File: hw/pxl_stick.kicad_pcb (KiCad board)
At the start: 2 copper layers, 25 x 99.9 mm, 69 parts, among them J1 Conn_01x02, J2 Conn_01x06_Socket, J3 Conn_01x01_Socket, J4 Conn_01x01, Q1 IRLML6244, Q2 IRLML6244, U1 AP2112K-3.3, U2 TSOP75438WTT, U3 INMP441ACEZ-R7, U4 ESP32-WROOM-E, U5 SN74LVC1T45DCK

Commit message: Version 1.1 changes
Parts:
- removed the G*** at (73.5, 55.5)
- removed the G*** at (69.6, 119.5)
- removed the G*** at (73.4, 119.4)
- removed the G*** at (81.0, 119.4)
- removed the G*** at (84.4, 99.7)
- removed NT3: NetTie_2, NetTie_Vasil:NetTie-2_SMD_Pad0.20mm
- removed the R5 at (66.5, 71.0)
- removed R6, R7: 510, Resistor_SMD:R_0805_2012Metric_Pad1.20x1.40mm_HandSolder
- removed TP1, TP2, TP3, TP8: TestPoint, TestPoint:TestPoint_Pad_1.0x1.0mm
- added C14: 100n, Capacitor_SMD:C_0805_2012Metric_Pad1.18x1.45mm_HandSolder, F.Cu at (62.4, 95.3)
- added R11: 20k, Resistor_SMD:R_0805_2012Metric_Pad1.20x1.40mm_HandSolder, F.Cu at (62.4, 99.1)
- added R12: 20k, Resistor_SMD:R_0805_2012Metric_Pad1.20x1.40mm_HandSolder, F.Cu at (84.5, 95.3)
- added ss1: qr, LOGO, B.Cu at (73.4, 50.5)
- C15: renamed from C14; value 100n -> 470n
- C16: renamed from C15; value 100n -> 470n
- J1: footprint Connector_Wire:SolderWire-0.15sqmm_1x02_P4mm_D0.5mm_OD1.5mm -> Connector_Wire:SolderWire-0.5sqmm_1x02_P4.6mm_D0.9mm_OD2.1mm
- J4: footprint Connector_Wire:SolderWire-0.15sqmm_1x01_D0.5mm_OD1.5mm -> Connector_Wire:SolderWire-0.5sqmm_1x01_D0.9mm_OD2.1mm
- R1: value 330 -> 470
- R15: renamed from R13; value 33 -> 430
- ss2: renamed from G***; value LOGO -> wled logo
- ss3: renamed from G***; value LOGO -> ws281x signal
- ss4: renamed from G***; value LOGO -> brightness
- ss5: renamed from G***; value LOGO -> palette
- ss6: renamed from G***; value LOGO -> reset
- ss7: renamed from G***; value LOGO -> bootloader
- moved C10 16.9 mm to (80.0, 71.1), turned to 90 degrees
- moved ss4 5.35 mm to (71.1, 119.8)
- moved G*** 4.46 mm to (78.3, 108.8)
- moved C9 3.65 mm to (66.7, 71.1), turned to 90 degrees
- moved ss5 1.50 mm to (75.7, 119.8)
- moved SW3 0.29 mm to (73.4, 58.0)
- moved ss3 0.24 mm to (78.4, 104.1)
- moved ss7 0.06 mm to (84.5, 91.8)
- turned JP2 to 90 degrees
- renumbered R11 to R13, R12 to R14, R2 to R3, R3 to R4, R4 to R5
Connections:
- D1 pad 2: +3V3 -> /MCU/LED
- SW1 pad 1: Net-(R5-Pad2) -> TB1
- SW2 pad 1: Net-(R6-Pad2) -> TB2
- SW3 pad 1: Net-(R7-Pad2) -> TB3
- U4 pad 13: unconnected-(U4-MTMS/GPIO14/ADC2_CH6-Pad13) -> TB3
- U4 pad 24: unconnected-(U4-ADC2_CH2/GPIO2-Pad24) -> /MCU/LED
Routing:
- net TB3: track 18.3 -> 61.1 mm, vias 0 -> 4
- net Net-(R6-Pad2): track 35.1 -> 0.00 mm
- net Net-(R5-Pad2): track 35.0 -> 0.00 mm
- net GND: track 115.3 -> 87.7 mm, vias 28 -> 21
- net Net-(R7-Pad2): track 24.2 -> 0.00 mm
- net TB2: track 44.7 -> 68.4 mm
- net TB1: track 31.0 -> 50.4 mm
- net /MCU/LED: track 0.00 -> 15.5 mm
- net /MCU/MCU_BOOT: track 45.6 -> 38.7 mm
- net +3V3: track 69.7 -> 65.4 mm, vias 10 -> 13
- net Net-(U2-VS): track 15.2 -> 12.6 mm
- net /MCU/MCU_EN: track 24.0 -> 26.3 mm
- net /MCU/WS2812_3V3: track 9.83 -> 8.17 mm, vias 2 -> 0
- net RE2: track 58.2 -> 56.6 mm
- net REB: track 47.7 -> 46.3 mm
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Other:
- outline, holes or cut-outs redrawn
- board text added: "PXL"
- board text added: "PXLstick"
- board text added: "WS281x | GPIO 4 󰝣 | GPIO 32 󰔷 | GPIO 33 󰄰 | GPIO 14 RE 1 | GPIO 27 RE 2 | GPIO 16 RE BTN | GPIO 17 LED | GPIO 2 IR rec | GPIO 23 MIC SD | GPIO 15 MIC WS | GPIO 13 MIC SCK | GPIO 25"
- board text added: "github.com/VasilKalchev/PXLstick"
- board text added: "v${REVISION}"
- board text added: "v${REVISION} ${ISSUE_DATE}"
- board text removed: "WLED"
- board text removed: "WLED stick"
- board text removed: "r${REVISION}"
- board text removed: "r1.0 2023-06-11"

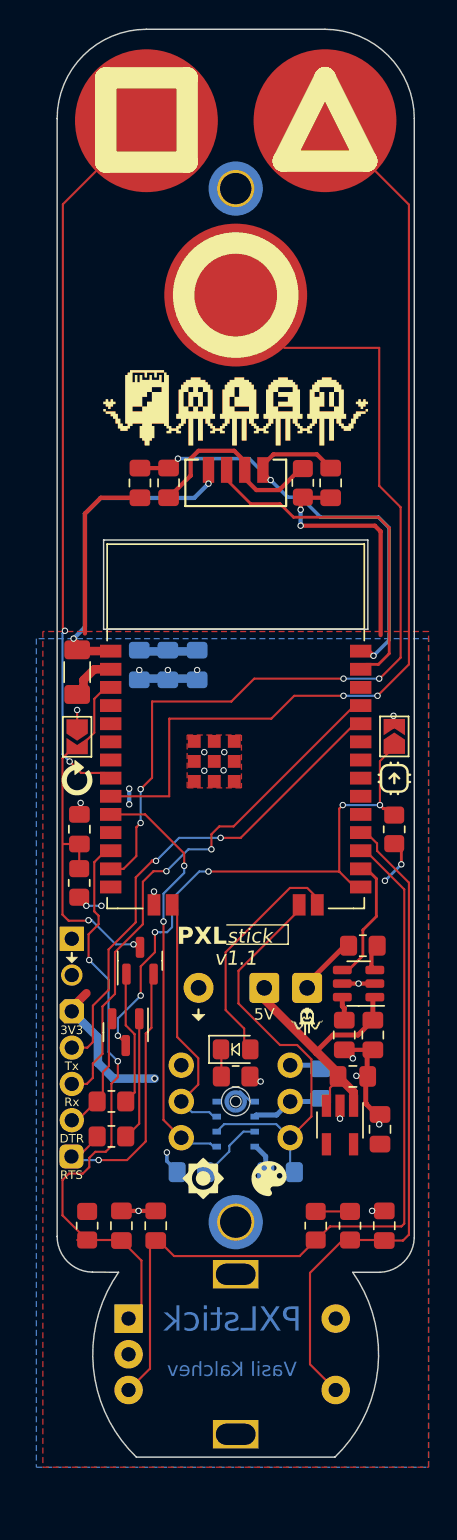
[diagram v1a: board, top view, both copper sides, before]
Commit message: Fix via annular width, remove netties
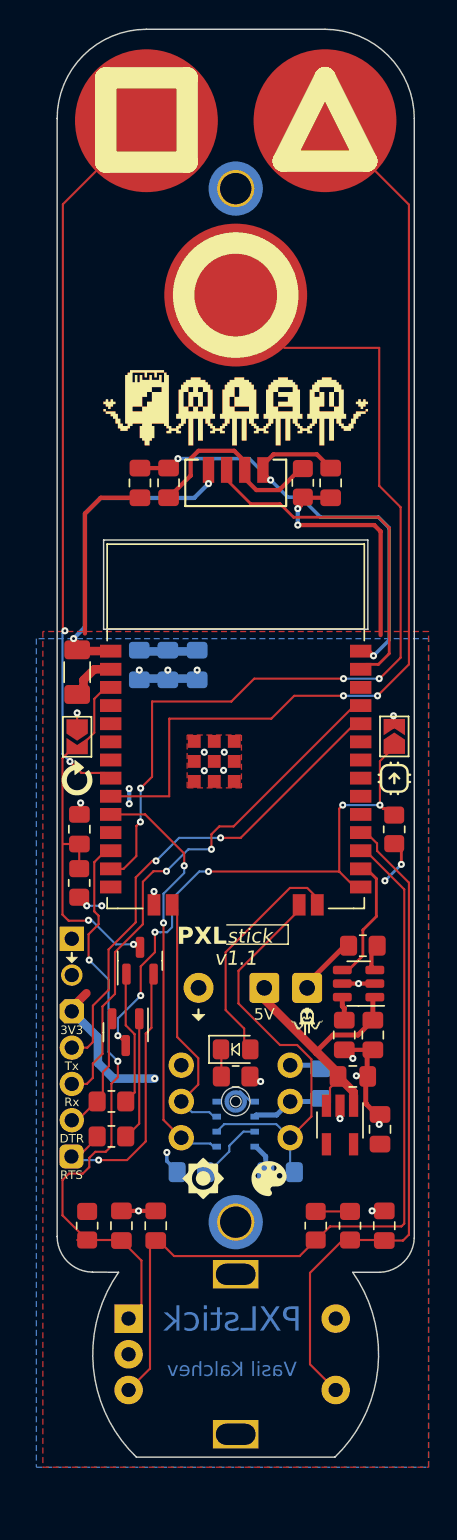
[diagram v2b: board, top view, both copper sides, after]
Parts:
- removed NT1, NT2: NetTie_2, NetTie_Vasil:NetTie-2_SMD_Pad0.20mm
- R13, R14, R3, R4, R5, R9: value 10k -> 20k
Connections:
- J2 pad 4: /MCU/SERIAL_TX -> /MCU/MCU_RX
- J2 pad 5: /MCU/SERIAL_RX -> /MCU/MCU_TX
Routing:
- net /MCU/MCU_RX: track 31.5 -> 34.1 mm
- net /MCU/MCU_TX: track 34.8 -> 37.1 mm
- net /MCU/SERIAL_TX: track 2.13 -> 0.00 mm
- net /MCU/SERIAL_RX: track 1.93 -> 0.00 mm

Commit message: change smalles hole to 0.3mm
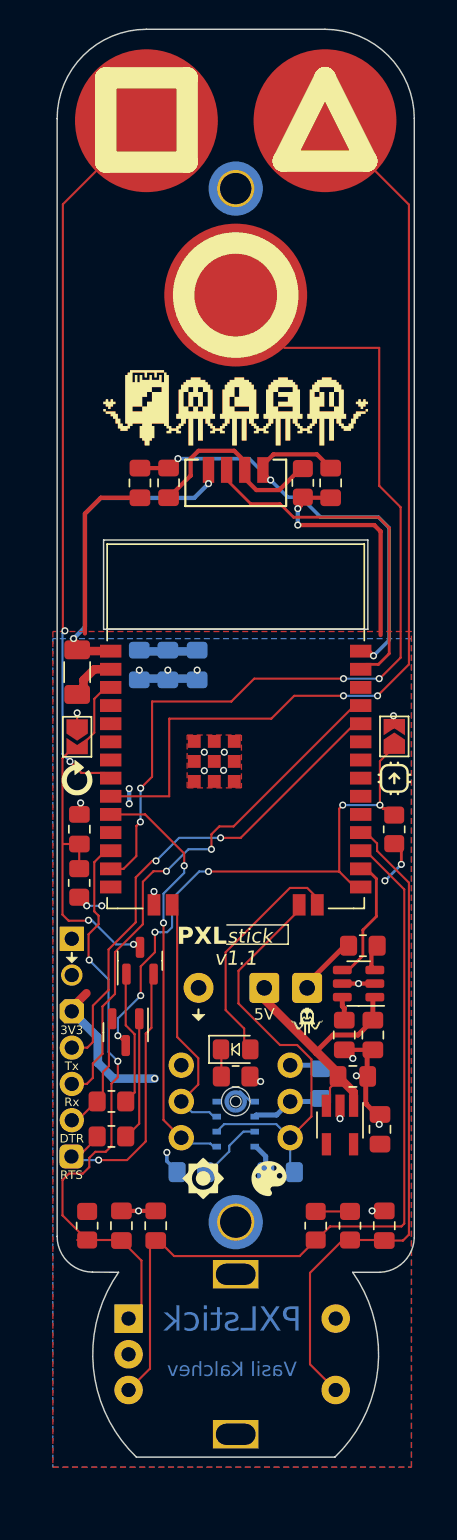
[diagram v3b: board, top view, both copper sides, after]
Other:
- board text removed: "Brightness | Speed | Intensity | Palette | Effect"
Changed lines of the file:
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@@
 				(material "Direct Printing")
 			)
-			(layer "F.Paste"
-				(type "Top Solder Paste")
-			)
 			(layer "F.Mask"
 				(type "Top Solder Mask")
@@
 				(loss_tangent 0)
 			)
-			(layer "B.Paste"
-				(type "Bottom Solder Paste")
-			)
 			(layer "B.SilkS"
 				(type "Bottom Silk Screen")
@@
 		)
 	)
-	(gr_text "Brightness | Speed | Intensity | Palette | Effect"
-		(at 167.9 130.9 0)
-		(layer "Cmts.User")
-		(effects
-			(font
-				(size 1 1)
-				(thickness 0.125)
-			)
-			(justify left bottom)
-		)
-	)
 	(dimension
 		(type aligned)
@@
 		(at 69.75 97.9)
 		(size 0.5)
-		(drill 0.2)
+		(drill 0.3)
 		(layers "F.Cu" "B.Cu")
 		(net 1)
@@
 		(at 68.3 101.9)
 		(size 0.5)
-		(drill 0.2)
+		(drill 0.3)
 		(layers "F.Cu" "B.Cu")
 		(net 1)
@@
 		(at 63.1 104.5)
 		(size 0.5)
-		(drill 0.2)
+		(drill 0.3)
 		(layers "F.Cu" "B.Cu")
 		(net 6)
@@
 		(at 65.104849 111.580973)
 		(size 0.5)
-		(drill 0.2)
+		(drill 0.3)
 		(layers "F.Cu" "B.Cu")
 		(net 6)
@@
 		(at 71.155349 89.944651)
 		(size 0.5)
-		(drill 0.2)
+		(drill 0.3)
 		(layers "F.Cu" "B.Cu")
 		(net 8)
@@
 		(at 62.5 93.5)
 		(size 0.5)
-		(drill 0.2)
+		(drill 0.3)
 		(layers "F.Cu" "B.Cu")
 		(net 8)
@@
 		(at 83.4 116)
 		(size 0.5)
-		(drill 0.2)
+		(drill 0.3)
 		(layers "F.Cu" "B.Cu")
 		(net 8)
@@
 		(at 62.005099 81.994901)
 		(size 0.5)
-		(drill 0.2)
+		(drill 0.3)
 		(layers "F.Cu" "B.Cu")
 		(net 8)
@@
 		(at 67.635349 99.7)
 		(size 0.5)
-		(drill 0.2)
+		(drill 0.3)
 		(layers "F.Cu" "B.Cu")
 		(net 8)
@@
 		(at 75.1 113)
 		(size 0.5)
-		(drill 0.2)
+		(drill 0.3)
 		(layers "F.Cu" "B.Cu")
 		(net 8)
@@
 		(at 80.655349 115.6)
 		(size 0.5)
-		(drill 0.2)
+		(drill 0.3)
 		(layers "F.Cu" "B.Cu")
 		(net 8)
@@
 		(at 69.3125 69.4)
 		(size 0.5)
-		(drill 0.2)
+		(drill 0.3)
 		(layers "F.Cu" "B.Cu")
 		(net 8)
@@
 		(at 81.8 112.6)
 		(size 0.5)
-		(drill 0.2)
+		(drill 0.3)
 		(layers "F.Cu" "B.Cu")
 		(net 8)
@@
 		(at 81.955349 106.144651)
 		(size 0.5)
-		(drill 0.2)
+		(drill 0.3)
 		(layers "F.Cu" "B.Cu")
 		(net 8)
@@
 		(at 83 83.2)
 		(size 0.5)
-		(drill 0.2)
+		(drill 0.3)
 		(layers "F.Cu" "B.Cu")
 		(net 8)
@@
 		(at 72.555349 89.944651)
 		(size 0.5)
-		(drill 0.2)
+		(drill 0.3)
 		(layers "F.Cu" "B.Cu")
 		(net 8)
@@
 		(at 72.505349 91.219651)
 		(size 0.5)
-		(drill 0.2)
+		(drill 0.3)
 		(layers "F.Cu" "B.Cu")
 		(net 8)
@@
 		(at 82.9 122.057151)
 		(size 0.5)
-		(drill 0.2)
+		(drill 0.3)
 		(layers "F.Cu" "B.Cu")
 		(net 8)
@@
 		(at 71.450349 71.149651)
 		(size 0.5)
-		(drill 0.2)
+		(drill 0.3)
 		(layers "F.Cu" "B.Cu")
 		(net 8)
@@
 		(at 62.255349 87.2)
 		(size 0.5)
-		(drill 0.2)
+		(drill 0.3)
 		(layers "F.Cu" "B.Cu")
 		(net 8)
@@
 		(at 75.8 70.9)
 		(size 0.5)
-		(drill 0.2)
+		(drill 0.3)
 		(layers "F.Cu" "B.Cu")
 		(net 8)
@@
 		(at 81.555349 111.382151)
 		(size 0.5)
-		(drill 0.2)
+		(drill 0.3)
 		(layers "F.Cu" "B.Cu")
 		(net 8)
@@
 		(at 71.155349 91.244651)
 		(size 0.5)
-		(drill 0.2)
+		(drill 0.3)
 		(layers "F.Cu" "B.Cu")
 		(net 8)
@@
 		(at 84.4 87.4)
 		(size 0.5)
-		(drill 0.2)
+		(drill 0.3)
 		(layers "F.Cu" "B.Cu")
 		(net 8)
@@
 		(at 66.555349 122.057151)
 		(size 0.5)
-		(drill 0.2)
+		(drill 0.3)
 		(layers "F.Cu" "B.Cu")
 		(net 8)
@@
 		(at 83.8 98.95)
 		(size 0.5)
-		(drill 0.2)
+		(drill 0.3)
 		(layers "F.Cu" "B.Cu")
 		(net 9)
@@
 		(at 70.655349 84.2)
 		(size 0.5)
-		(drill 0.2)
+		(drill 0.3)
 		(layers "F.Cu" "B.Cu")
 		(net 9)
@@
 		(at 77.7 74.05)
 		(size 0.5)
-		(drill 0.2)
+		(drill 0.3)
 		(layers "F.Cu" "B.Cu")
 		(net 9)
@@
 		(at 66.605349 84.2)
 		(size 0.5)
-		(drill 0.2)
+		(drill 0.3)
 		(layers "F.Cu" "B.Cu")
 		(net 9)
@@
 		(at 68.536638 117.963674)
 		(size 0.5)
-		(drill 0.2)
+		(drill 0.3)
 		(layers "F.Cu" "B.Cu")
 		(net 9)
@@
 		(at 68.605349 84.2)
 		(size 0.5)
-		(drill 0.2)
+		(drill 0.3)
 		(layers "F.Cu" "B.Cu")
 		(net 9)
@@
 		(at 63.980349 100.7)
 		(size 0.5)
-		(drill 0.2)
+		(drill 0.3)
 		(layers "F.Cu" "B.Cu")
 		(net 9)
@@
 		(at 84.95 97.8)
 		(size 0.5)
-		(drill 0.2)
+		(drill 0.3)
 		(layers "F.Cu" "B.Cu")
 		(net 9)
@@
 		(at 65.9 93.559651)
 		(size 0.5)
-		(drill 0.2)
+		(drill 0.3)
 		(layers "F.Cu" "B.Cu")
 		(net 9)
@@
 		(at 67.679849 112.794651)
 		(size 0.5)
-		(drill 0.2)
+		(drill 0.3)
 		(layers "F.Cu" "B.Cu")
 		(net 9)
@@
 		(at 65.9 92.5)
 		(size 0.5)
-		(drill 0.2)
+		(drill 0.3)
 		(layers "F.Cu" "B.Cu")
 		(free yes)
@@
 		(at 62.930349 100.7)
 		(size 0.5)
-		(drill 0.2)
+		(drill 0.3)
 		(layers "F.Cu" "B.Cu")
 		(net 9)
@@
 		(at 77.7 72.9)
 		(size 0.5)
-		(drill 0.2)
+		(drill 0.3)
 		(layers "F.Cu" "B.Cu")
 		(net 9)
@@
 		(at 63.761582 118.500884)
 		(size 0.5)
-		(drill 0.2)
+		(drill 0.3)
 		(layers "F.Cu" "B.Cu")
 		(net 19)
@@
 		(at 71.655349 96.744651)
 		(size 0.5)
-		(drill 0.2)
+		(drill 0.3)
 		(layers "F.Cu" "B.Cu")
 		(net 20)
@@
 		(at 68.505349 98.281438)
 		(size 0.5)
-		(drill 0.2)
+		(drill 0.3)
 		(layers "F.Cu" "B.Cu")
 		(net 20)
@@
 		(at 72.3 95.944651)
 		(size 0.5)
-		(drill 0.2)
+		(drill 0.3)
 		(layers "F.Cu" "B.Cu")
 		(net 21)
@@
 		(at 67.778112 97.556938)
 		(size 0.5)
-		(drill 0.2)
+		(drill 0.3)
 		(layers "F.Cu" "B.Cu")
 		(net 21)
@@
 		(at 83.284331 86.000578)
 		(size 0.5)
-		(drill 0.2)
+		(drill 0.3)
 		(layers "F.Cu" "B.Cu")
 		(net 28)
@@
 		(at 80.9 86)
 		(size 0.5)
-		(drill 0.2)
+		(drill 0.3)
 		(layers "F.Cu" "B.Cu")
 		(net 28)
@@
 		(at 66.7 92.467326)
 		(size 0.5)
-		(drill 0.2)
+		(drill 0.3)
 		(layers "F.Cu" "B.Cu")
 		(net 29)
@@
 		(at 83.4 84.8)
 		(size 0.5)
-		(drill 0.2)
+		(drill 0.3)
 		(layers "F.Cu" "B.Cu")
 		(net 29)
@@
 		(at 66.684117 94.829651)
 		(size 0.5)
-		(drill 0.2)
+		(drill 0.3)
 		(layers "F.Cu" "B.Cu")
 		(net 29)
@@
 		(at 80.9 84.8)
 		(size 0.5)
-		(drill 0.2)
+		(drill 0.3)
 		(layers "F.Cu" "B.Cu")
 		(net 29)
@@
 		(at 61.4 81.45)
 		(size 0.5)
-		(drill 0.2)
+		(drill 0.3)
 		(layers "F.Cu" "B.Cu")
 		(net 30)
@@
 		(at 61.755349 90.6)
 		(size 0.5)
-		(drill 0.2)
+		(drill 0.3)
 		(layers "F.Cu" "B.Cu")
 		(net 30)
@@
 		(at 63.04974 101.712503)
 		(size 0.5)
-		(drill 0.2)
+		(drill 0.3)
 		(layers "F.Cu" "B.Cu")
 		(net 32)
@@
 		(at 66.2 103.4)
 		(size 0.5)
-		(drill 0.2)
+		(drill 0.3)
 		(layers "F.Cu" "B.Cu")
 		(net 32)
@@
 		(at 66.705349 106.986509)
 		(size 0.5)
-		(drill 0.2)
+		(drill 0.3)
 		(layers "F.Cu" "B.Cu")
 		(net 35)
@@
 		(at 83.45 93.65)
 		(size 0.5)
-		(drill 0.2)
+		(drill 0.3)
 		(layers "F.Cu" "B.Cu")
 		(net 35)
@@
 		(at 71.45 98.3)
 		(size 0.5)
-		(drill 0.2)
+		(drill 0.3)
 		(layers "F.Cu" "B.Cu")
 		(net 35)
@@
 		(at 80.85 93.65)
 		(size 0.5)
-		(drill 0.2)
+		(drill 0.3)
 		(layers "F.Cu" "B.Cu")
 		(net 35)
@@
 		(at 67.700419 102.545492)
 		(size 0.5)
-		(drill 0.2)
+		(drill 0.3)
 		(layers "F.Cu" "B.Cu")
 		(net 35)
@@
 		(at 65.107782 109.79309)
 		(size 0.5)
-		(drill 0.2)
+		(drill 0.3)
 		(layers "F.Cu" "B.Cu")
 		(net 35)
@@
 		(polygon
 			(pts
-				(xy 86.855349 140) (xy 86.855349 81.5) (xy 59.855349 81.5) (xy 59.855349 140)
+				(xy 85.655349 140) (xy 85.655349 81.5) (xy 60.555349 81.5) (xy 60.555349 140)
 			)
 		)
@@
 		(polygon
 			(pts
-				(xy 59.4 140) (xy 86.855349 140) (xy 86.855349 82) (xy 59.4 82)
+				(xy 60.55 140) (xy 85.655349 140) (xy 85.655349 82) (xy 60.55 82)
 			)
 		)
